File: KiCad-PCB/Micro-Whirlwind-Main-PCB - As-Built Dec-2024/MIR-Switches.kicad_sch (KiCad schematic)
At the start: 29 parts, among them SW1 mSW_Push_LEDx8, SW10 SW_Push_LED, SW11 SW_Push_LED, SW12 SW_Push_LED, SW13 SW_Push_LED, SW14 SW_Push_LED, SW15 SW_Push_LED, SW18 mSW_Push_LEDx8, SW19 mSW_Push_LEDx8, SW2 mSW_Push_LEDx8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

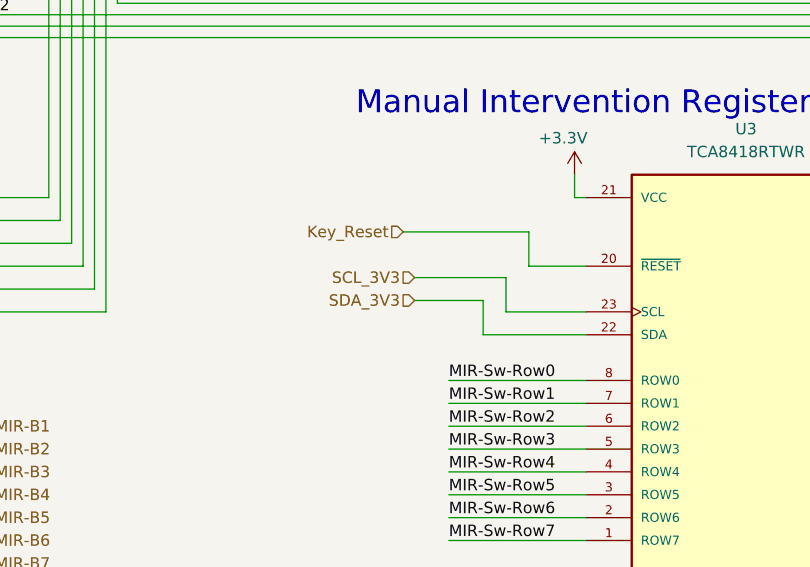
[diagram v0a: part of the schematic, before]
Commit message: I made most of the corrections to the schematic and some to the PCB. The Main PCB needs to be redone with a four-layer PCB, so I didn't re-route all the traces on the PCB The Power switch needs to be moved out of the way of the HDMI connector - that wasn't done either. See Notes/PCB-Corrections for a listing of the changes made, and the ones that are still pending   /guy
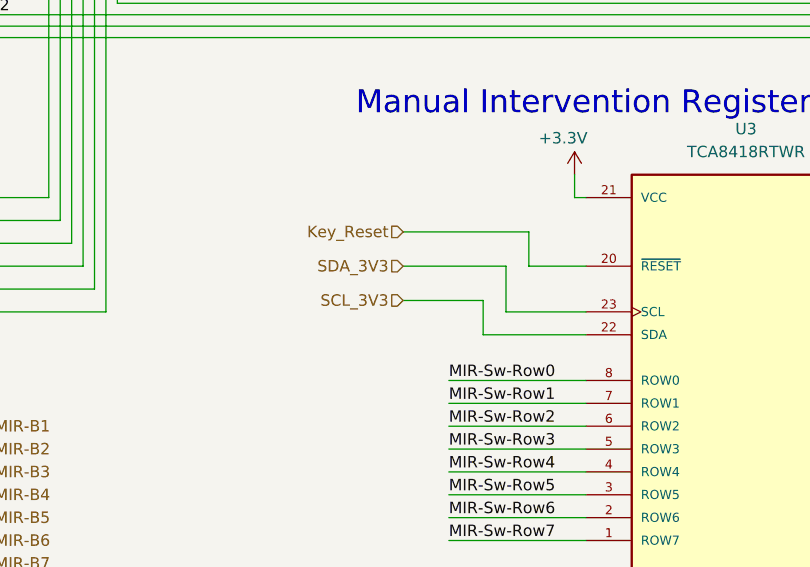
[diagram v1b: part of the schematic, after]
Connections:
- net SCL_3V3: now also U3.22 (SDA); no longer U3.23 (SCL)
- net SDA_3V3: now also U3.23 (SCL); no longer U3.22 (SDA)
